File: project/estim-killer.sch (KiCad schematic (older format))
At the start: 4 parts

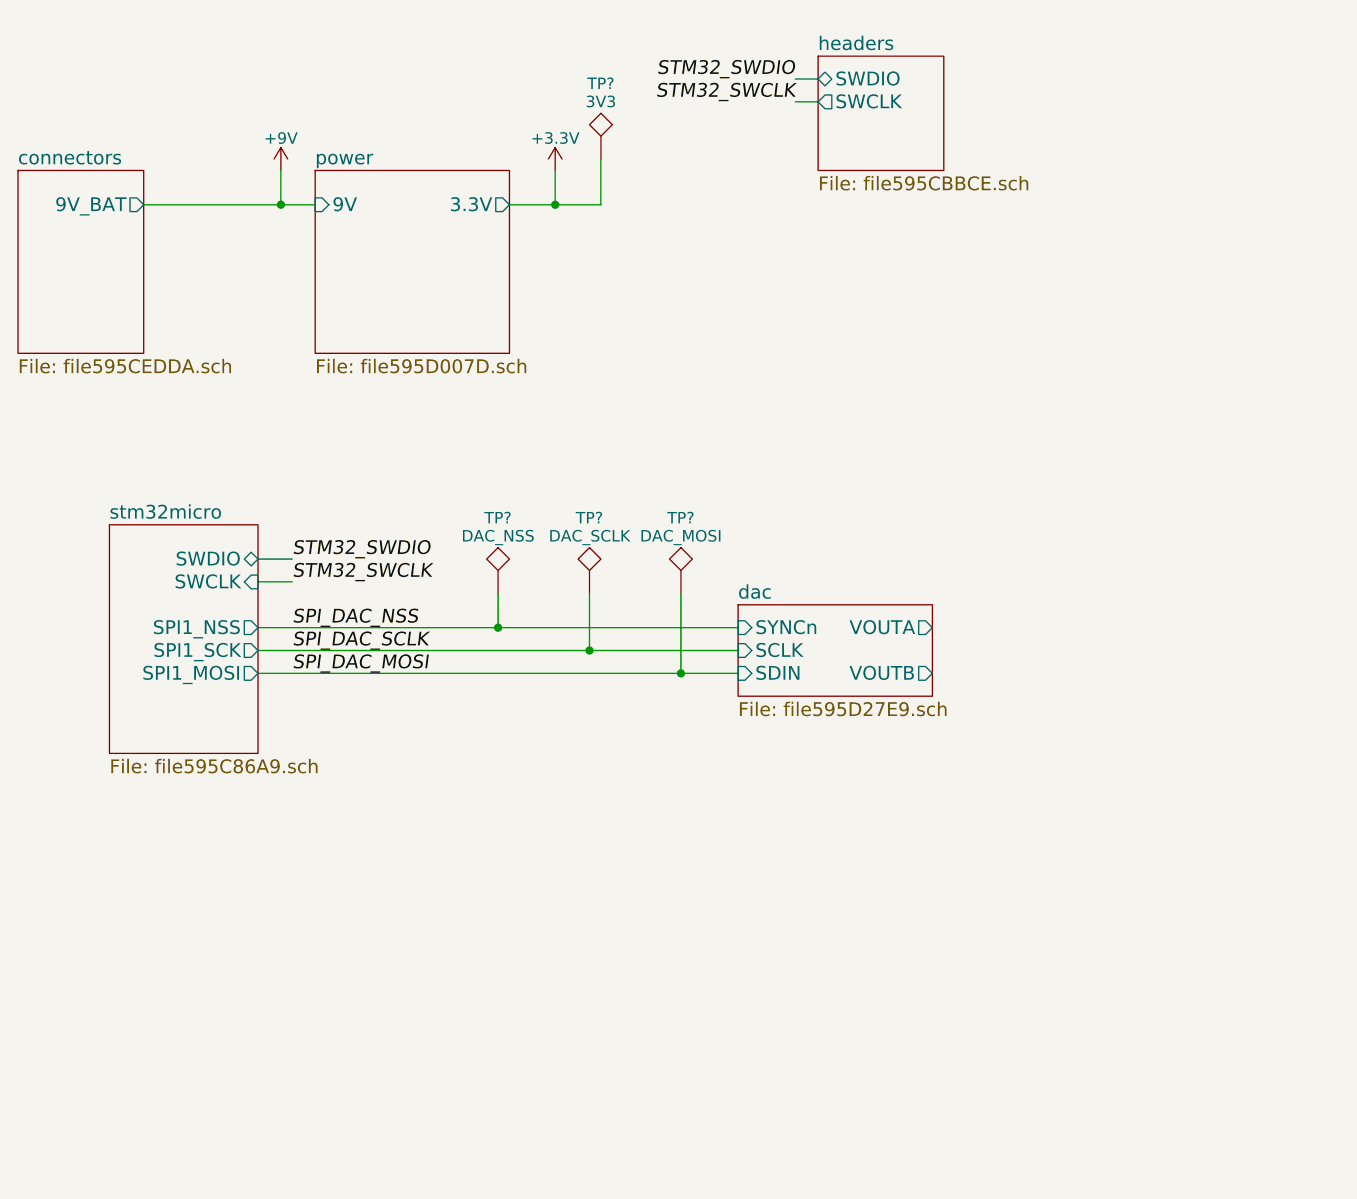
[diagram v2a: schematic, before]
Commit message: Add digital potentiometer (TPL0102-100) to schematic.
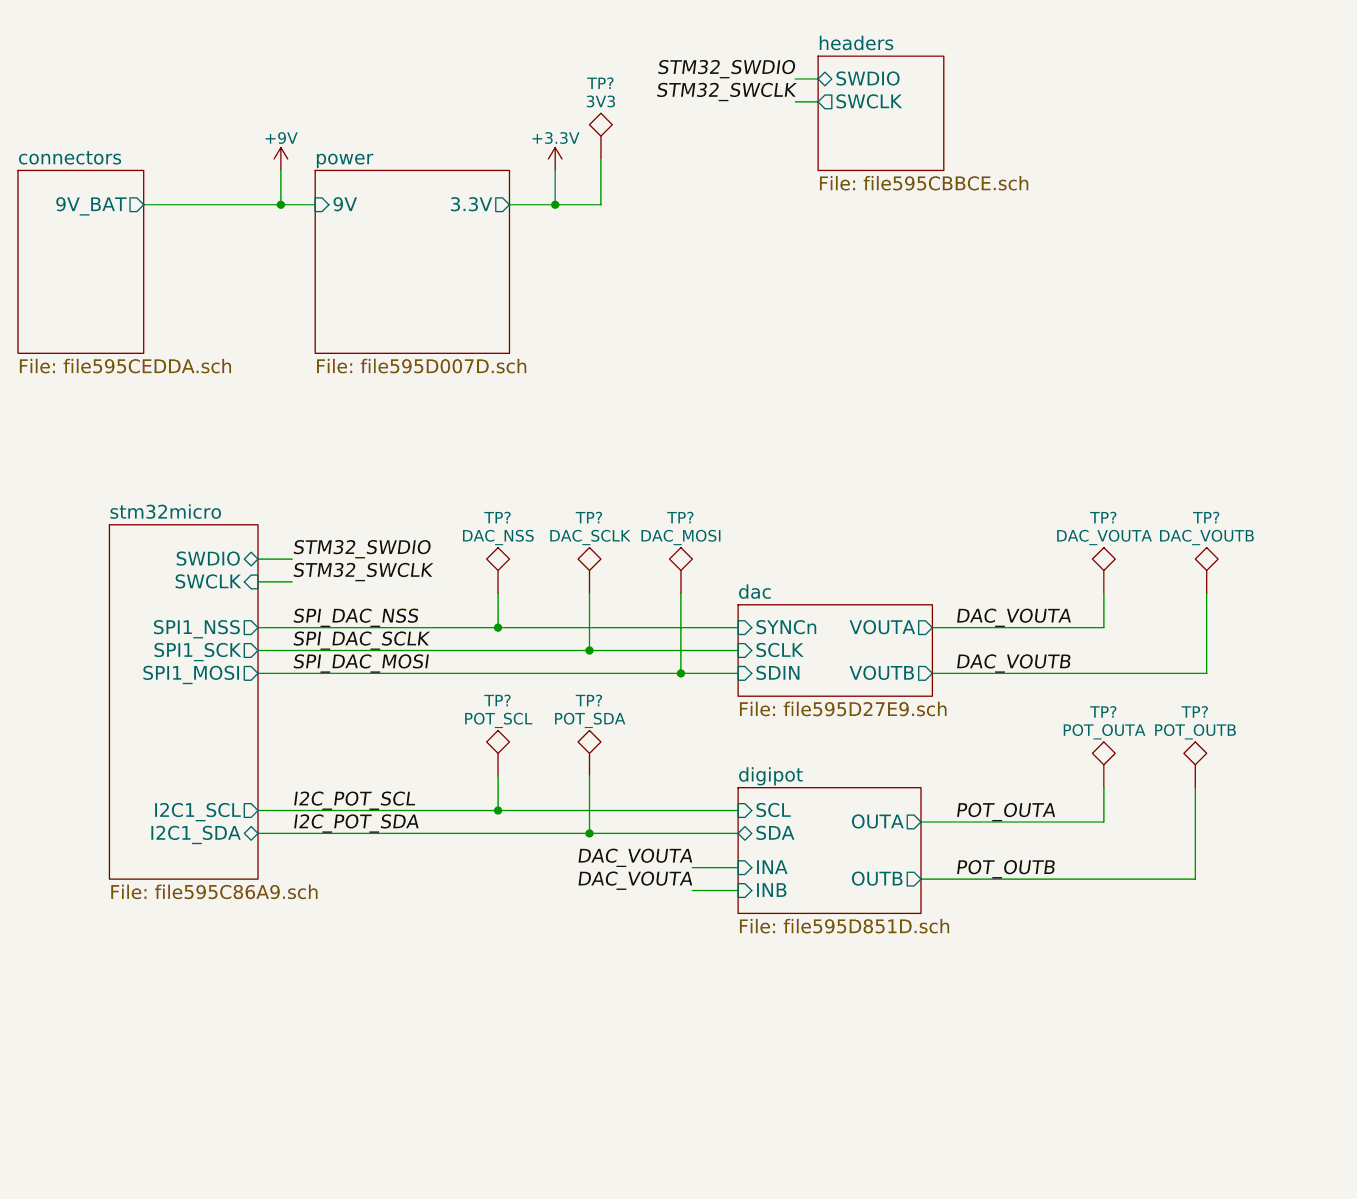
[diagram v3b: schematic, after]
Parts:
- added TP?: DAC_VOUTA, Measurement_Points:Measurement_Point_Round-SMD-Pad_Small, symbol TEST
- added TP?: DAC_VOUTB, Measurement_Points:Measurement_Point_Round-SMD-Pad_Small, symbol TEST
- added TP?: POT_SCL, Measurement_Points:Measurement_Point_Round-SMD-Pad_Small, symbol TEST
- added TP?: POT_SDA, Measurement_Points:Measurement_Point_Round-SMD-Pad_Small, symbol TEST
- added TP?: POT_OUTA, Measurement_Points:Measurement_Point_Round-SMD-Pad_Small, symbol TEST
- added TP?: POT_OUTB, Measurement_Points:Measurement_Point_Round-SMD-Pad_Small, symbol TEST
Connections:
- new net DAC_VOUTA: TP?.1
- new net DAC_VOUTB: TP?.1
- new net I2C_POT_SCL: TP?.1
- new net I2C_POT_SDA: TP?.1
- new net POT_OUTA: TP?.1
- new net POT_OUTB: TP?.1
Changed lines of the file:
@@
 $Descr A4 11693 8268
 encoding utf-8
-Sheet 1 6
+Sheet 1 7
 Title ""
 Date ""
@@
 $EndDescr
 $Sheet
-S 1250 2900 650  1000
+S 1250 2900 650  1550
 U 595C86AA
 F0 "stm32micro" 60
@@
 F5 "SPI1_SCK" O R 1900 3450 60
 F6 "SPI1_MOSI" O R 1900 3550 60
+F7 "I2C1_SCL" O R 1900 4150 60
+F8 "I2C1_SDA" B R 1900 4250 60
 $EndSheet
 $Sheet
@@
 Wire Wire Line
 	2050 3150 1900 3150
+Text Label 4950 3350 0    60   Italic 0
+DAC_VOUTA
+Text Label 4950 3550 0    60   Italic 0
+DAC_VOUTB
+$Comp
+L TEST TP?
+U 1 1 595D7FBD
+P 5600 3200
+F 0 "TP?" H 5600 3500 50  0000 C BNN
+F 1 "DAC_VOUTA" H 5600 3450 50  0000 C CNN
+F 2 "Measurement_Points:Measurement_Point_Round-SMD-Pad_Small" H 5600 3200 50  0001 C CNN
+F 3 "" H 5600 3200 50  0001 C CNN
+	1    5600 3200
+	1    0    0    -1
+$EndComp
+$Comp
+L TEST TP?
+U 1 1 595D8168
+P 6050 3200
+F 0 "TP?" H 6050 3500 50  0000 C BNN
+F 1 "DAC_VOUTB" H 6050 3450 50  0000 C CNN
+F 2 "Measurement_Points:Measurement_Point_Round-SMD-Pad_Small" H 6050 3200 50  0001 C CNN
+F 3 "" H 6050 3200 50  0001 C CNN
+	1    6050 3200
+	1    0    0    -1
+$EndComp
+Wire Wire Line
+	4850 3350 5600 3350
+Wire Wire Line
+	5600 3350 5600 3200
+Wire Wire Line
+	4850 3550 6050 3550
+Wire Wire Line
+	6050 3550 6050 3200
+$Sheet
+S 4000 4050 800  550
+U 595D851E
+F0 "digipot" 60
+F1 "file595D851D.sch" 60
+F2 "SCL" I L 4000 4150 60
+F3 "SDA" B L 4000 4250 60
+F4 "OUTB" O R 4800 4450 60
+F5 "OUTA" O R 4800 4200 60
+F6 "INA" I L 4000 4400 60
+F7 "INB" I L 4000 4500 60
+$EndSheet
+Wire Wire Line
+	1900 4150 4000 4150
+Wire Wire Line
+	1900 4250 4000 4250
+Text Label 2050 4150 0    60   Italic 0
+I2C_POT_SCL
+Text Label 2050 4250 0    60   Italic 0
+I2C_POT_SDA
+$Comp
+L TEST TP?
+U 1 1 595DAB2D
+P 2950 4000
+F 0 "TP?" H 2950 4300 50  0000 C BNN
+F 1 "POT_SCL" H 2950 4250 50  0000 C CNN
+F 2 "Measurement_Points:Measurement_Point_Round-SMD-Pad_Small" H 2950 4000 50  0001 C CNN
+F 3 "" H 2950 4000 50  0001 C CNN
+	1    2950 4000
+	1    0    0    -1
+$EndComp
+$Comp
+L TEST TP?
+U 1 1 595DAC9B
+P 3350 4000
+F 0 "TP?" H 3350 4300 50  0000 C BNN
+F 1 "POT_SDA" H 3350 4250 50  0000 C CNN
+F 2 "Measurement_Points:Measurement_Point_Round-SMD-Pad_Small" H 3350 4000 50  0001 C CNN
+F 3 "" H 3350 4000 50  0001 C CNN
+	1    3350 4000
+	1    0    0    -1
+$EndComp
+Wire Wire Line
+	2950 4000 2950 4150
+Connection ~ 2950 4150
+Wire Wire Line
+	3350 4000 3350 4250
+Connection ~ 3350 4250
+Text Label 3800 4400 2    60   Italic 0
+DAC_VOUTA
+Wire Wire Line
+	3800 4400 4000 4400
+Text Label 3800 4500 2    60   Italic 0
+DAC_VOUTA
+Wire Wire Line
+	3800 4500 4000 4500
+Text Label 4950 4200 0    60   Italic 0
+POT_OUTA
+Text Label 4950 4450 0    60   Italic 0
+POT_OUTB
+$Comp
+L TEST TP?
+U 1 1 595DBFA6
+P 5600 4050
+F 0 "TP?" H 5600 4350 50  0000 C BNN
+F 1 "POT_OUTA" H 5600 4300 50  0000 C CNN
+F 2 "Measurement_Points:Measurement_Point_Round-SMD-Pad_Small" H 5600 4050 50  0001 C CNN
+F 3 "" H 5600 4050 50  0001 C CNN
+	1    5600 4050
+	1    0    0    -1
+$EndComp
+$Comp
+L TEST TP?
+U 1 1 595DC272
+P 6000 4050
+F 0 "TP?" H 6000 4350 50  0000 C BNN
+F 1 "POT_OUTB" H 6000 4300 50  0000 C CNN
+F 2 "Measurement_Points:Measurement_Point_Round-SMD-Pad_Small" H 6000 4050 50  0001 C CNN
+F 3 "" H 6000 4050 50  0001 C CNN
+	1    6000 4050
+	1    0    0    -1
+$EndComp
+Wire Wire Line
+	4800 4200 5600 4200
+Wire Wire Line
+	5600 4200 5600 4050
+Wire Wire Line
+	4800 4450 6000 4450
+Wire Wire Line
+	6000 4450 6000 4050
 $EndSCHEMATC

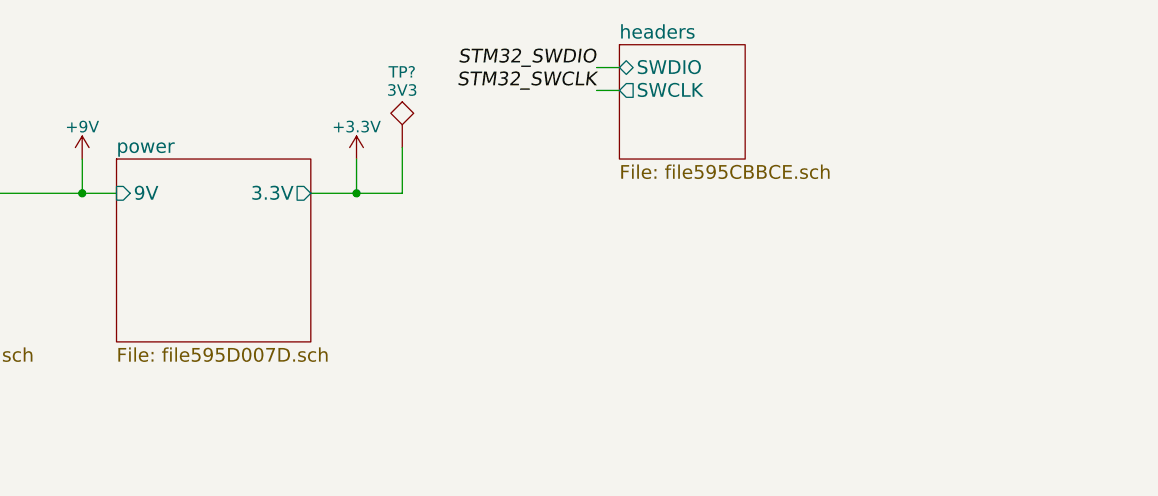
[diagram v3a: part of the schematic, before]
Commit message: Update README with links to documentation for all parts entered in schematic so far. Add 9V to 14V boost converter for output amplifier to schematic.
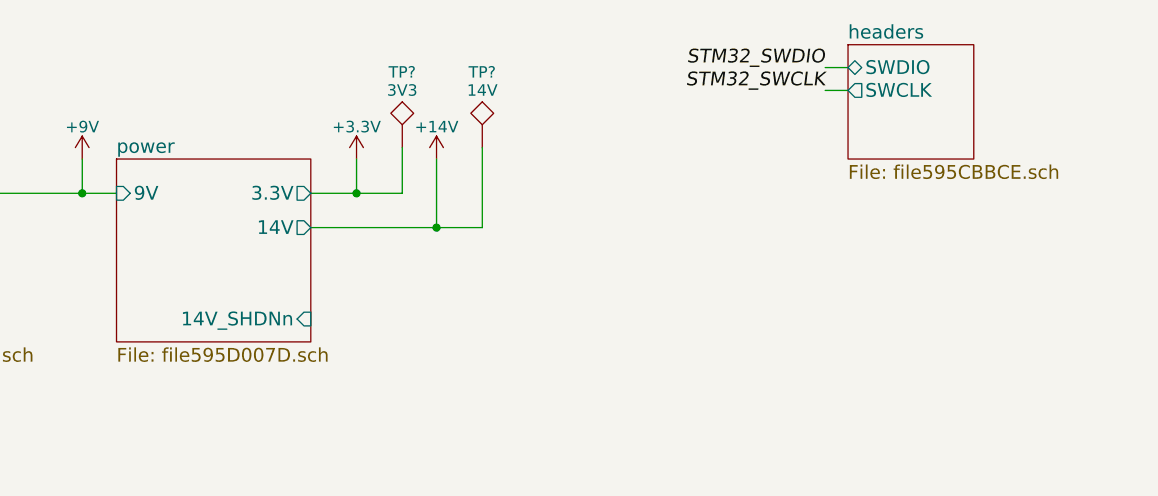
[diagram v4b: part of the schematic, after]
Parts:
- added TP?: 14V, Measurement_Points:Measurement_Point_Round-SMD-Pad_Small, symbol TEST
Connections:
- new net +14V: TP?.1
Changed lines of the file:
@@
 $EndSheet
 $Sheet
-S 4350 850  550  500
+S 5350 850  550  500
 U 595CBBCF
 F0 "headers" 60
 F1 "file595CBBCE.sch" 60
-F2 "SWDIO" B L 4350 950 60
-F3 "SWCLK" O L 4350 1050 60
-$EndSheet
-Text Label 4250 950  2    60   Italic 0
+F2 "SWDIO" B L 5350 950 60
+F3 "SWCLK" O L 5350 1050 60
+$EndSheet
+Text Label 5250 950  2    60   Italic 0
 STM32_SWDIO
-Text Label 4250 1050 2    60   Italic 0
+Text Label 5250 1050 2    60   Italic 0
 STM32_SWCLK
-Wire Wire Line
-	4250 1050 4350 1050
-Wire Wire Line
-	4250 950  4350 950
 Text Label 2050 3050 0    60   Italic 0
 STM32_SWDIO
@@
 F2 "3.3V" O R 3000 1500 60
 F3 "9V" I L 2150 1500 60
-$EndSheet
-Wire Wire Line
-	1400 1500 2150 1500
+F4 "14V" O R 3000 1650 60
+F5 "14V_SHDNn" I R 3000 2050 60
+$EndSheet
 $Comp
 L +9V #PWR01
@@
 	1    0    0    -1
 $EndComp
-Wire Wire Line
-	2000 1350 2000 1500
-Connection ~ 2000 1500
 $Comp
 L +3.3V #PWR02
@@
 	1    0    0    -1
 $EndComp
-Wire Wire Line
-	3000 1500 3400 1500
-Wire Wire Line
-	3400 1500 3400 1300
-Wire Wire Line
-	3200 1350 3200 1500
-Connection ~ 3200 1500
 $Sheet
 S 4000 3250 850  400
@@
 F6 "SCLK" I L 4000 3450 60
 $EndSheet
-Wire Wire Line
-	1900 3350 4000 3350
 Text Label 2050 3350 0    60   Italic 0
 SPI_DAC_NSS
-Wire Wire Line
-	1900 3450 4000 3450
 Text Label 2050 3450 0    60   Italic 0
 SPI_DAC_SCLK
 Text Label 2050 3550 0    60   Italic 0
 SPI_DAC_MOSI
-Wire Wire Line
-	1900 3550 4000 3550
 $Comp
 L TEST TP?
@@
 	1    0    0    -1
 $EndComp
-Wire Wire Line
-	2950 3200 2950 3350
-Connection ~ 2950 3350
-Wire Wire Line
-	3350 3200 3350 3450
-Connection ~ 3350 3450
-Wire Wire Line
-	3750 3200 3750 3550
-Connection ~ 3750 3550
-Wire Wire Line
-	1900 3050 2050 3050
-Wire Wire Line
-	2050 3150 1900 3150
 Text Label 4950 3350 0    60   Italic 0
 DAC_VOUTA
@@
 	1    0    0    -1
 $EndComp
-Wire Wire Line
-	4850 3350 5600 3350
-Wire Wire Line
-	5600 3350 5600 3200
-Wire Wire Line
-	4850 3550 6050 3550
-Wire Wire Line
-	6050 3550 6050 3200
 $Sheet
 S 4000 4050 800  550
@@
 F7 "INB" I L 4000 4500 60
 $EndSheet
-Wire Wire Line
-	1900 4150 4000 4150
-Wire Wire Line
-	1900 4250 4000 4250
 Text Label 2050 4150 0    60   Italic 0
 I2C_POT_SCL
@@
 	1    0    0    -1
 $EndComp
-Wire Wire Line
-	2950 4000 2950 4150
-Connection ~ 2950 4150
-Wire Wire Line
-	3350 4000 3350 4250
-Connection ~ 3350 4250
 Text Label 3800 4400 2    60   Italic 0
 DAC_VOUTA
-Wire Wire Line
-	3800 4400 4000 4400
 Text Label 3800 4500 2    60   Italic 0
 DAC_VOUTA
-Wire Wire Line
-	3800 4500 4000 4500
 Text Label 4950 4200 0    60   Italic 0
 POT_OUTA
@@
 	1    0    0    -1
 $EndComp
+$Comp
+L TEST TP?
+U 1 1 595CFC49
+P 3750 1300
+F 0 "TP?" H 3750 1600 50  0000 C BNN
+F 1 "14V" H 3750 1550 50  0000 C CNN
+F 2 "Measurement_Points:Measurement_Point_Round-SMD-Pad_Small" H 3750 1300 50  0001 C CNN
+F 3 "" H 3750 1300 50  0001 C CNN
+	1    3750 1300
+	1    0    0    -1
+$EndComp
+$Comp
+L +14V #PWR?
+U 1 1 595D02BE
+P 3550 1350
+F 0 "#PWR?" H 3550 1200 50  0001 C CNN
+F 1 "+14V" H 3550 1490 50  0000 C CNN
+F 2 "" H 3550 1350 50  0001 C CNN
+F 3 "" H 3550 1350 50  0001 C CNN
+	1    3550 1350
+	1    0    0    -1
+$EndComp
+Wire Wire Line
+	5250 1050 5350 1050
+Wire Wire Line
+	5250 950  5350 950
+Wire Wire Line
+	1400 1500 2150 1500
+Wire Wire Line
+	2000 1350 2000 1500
+Connection ~ 2000 1500
+Wire Wire Line
+	3000 1500 3400 1500
+Wire Wire Line
+	3400 1500 3400 1300
+Wire Wire Line
+	3200 1350 3200 1500
+Connection ~ 3200 1500
+Wire Wire Line
+	1900 3350 4000 3350
+Wire Wire Line
+	1900 3450 4000 3450
+Wire Wire Line
+	1900 3550 4000 3550
+Wire Wire Line
+	2950 3200 2950 3350
+Connection ~ 2950 3350
+Wire Wire Line
+	3350 3200 3350 3450
+Connection ~ 3350 3450
+Wire Wire Line
+	3750 3200 3750 3550
+Connection ~ 3750 3550
+Wire Wire Line
+	1900 3050 2050 3050
+Wire Wire Line
+	2050 3150 1900 3150
+Wire Wire Line
+	4850 3350 5600 3350
+Wire Wire Line
+	5600 3350 5600 3200
+Wire Wire Line
+	4850 3550 6050 3550
+Wire Wire Line
+	6050 3550 6050 3200
+Wire Wire Line
+	1900 4150 4000 4150
+Wire Wire Line
+	1900 4250 4000 4250
+Wire Wire Line
+	2950 4000 2950 4150
+Connection ~ 2950 4150
+Wire Wire Line
+	3350 4000 3350 4250
+Connection ~ 3350 4250
+Wire Wire Line
+	3800 4400 4000 4400
+Wire Wire Line
+	3800 4500 4000 4500
 Wire Wire Line
 	4800 4200 5600 4200
@@
 Wire Wire Line
 	6000 4450 6000 4050
+Wire Wire Line
+	3000 1650 3750 1650
+Wire Wire Line
+	3750 1650 3750 1300
+Wire Wire Line
+	3550 1350 3550 1650
+Connection ~ 3550 1650
 $EndSCHEMATC
